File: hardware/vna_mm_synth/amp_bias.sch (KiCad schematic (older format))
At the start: 108 parts, among them U201 LTC2937, U202 NCP692, U203 ADP7158, U204 LM2776, U205 LTM4622A, U206 TPS22918, U207 TPS22918, U208 TPS22918, U209 TPS72301DB, U210 TPS72301DB, U211 TPS72301DB

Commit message: changed synth midband filter bank to admv8416, added rf test points
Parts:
- removed R234: 0, Resistors_SMD:R_0402, symbol Device:R_Small
- added R252, R253: DNI, Resistors_SMD:R_0402, symbol Device:R_Small
- C1120, C1121: DIST_PN (none) -> 399-5514-1-ND
- C229, C230, C231: value C_Small -> 1 uF
- C235, C236, C237: value C_Small -> DNI
- D201: DIST_PN (none) -> 511-1581-1-ND‎
- L201, L202: value L_Small -> BLM15GG471
- R1119: value JMP -> 0
- R1120: value TBD -> 7.5k
- R1122: value TBD -> 12k
- R240, R241, R242: value R_Small -> 10k
- R243, R244, R245: value R_Small -> 1k
- R246, R250: value R_Small -> 68k
- R247: value R_Small -> 21k; DIST_PN (none) -> 311-21.0KLRCT-ND‎
- R248: value R_Small -> 51k
- R249: value R_Small -> 47k
- R251: value R_Small -> 39k
- U201: DIST_PN (none) -> ‎LTC2937CUHE#PBF-ND‎
- U202: DIST_PN (none) -> NCP692MN50T2GOSCT-ND
- U203: DIST_PN (none) -> ADP7158ACPZ-3.3-R7CT-ND‎
- U204: footprint Package_TO_SOT_SMD:SOT-23-6 -> TO_SOT_Packages_SMD:SOT-23-6; DIST_PN (none) -> 296-43957-1-ND
- U205: DIST_PN (none) -> ‎LTM4622AEY#PBF-ND‎
- U206, U207, U208: DIST_PN (none) -> 296-46278-1-ND
- U209, U210, U211: DIST_PN (none) -> ‎296-46478-1-ND‎
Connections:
- net GND: now also R252.2, R253.2
- net PMIC_SDA: no longer R1103.2, U201.19 (SCL)
- net at U204.1 (VOUT): now also C1111.2, C1115.2, L202.2, R236.1
- net at U201.6 (ASEL1): now also R252.1
- net at U201.8 (ASEL3): now also R253.1
- new net PMIC_SCL: R1103.2, U201.19 (SCL)
- no-connect marks 6 -> 4
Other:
- note added: "Rfb = 60.4k * (0.6 / (Vout - 0.6))"

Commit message: added trl cal and set of breakout boards
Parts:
- renumbered C1112 to C1110, C1114 to C1111, C1118 to C1112, C1116 to C1113, C1113 to C1114, C1117 to C1115, C1110 to C1116, C1119 to C1117, C1120 to C1118, C1121 to C1119, C1122 to C1120, C1123 to C1121, C1115 to C1122, C1111 to C1123, C226 to C1126, C227 to C1127, C228 to C1128, C229 to C1129, C230 to C1130, C231 to C1131, C232 to C1132, C233 to C1133, C234 to C1134, C235 to C1135, C236 to C1136, C237 to C1137, C238 to C1138, C239 to C1139, C240 to C1140, C241 to C1141, C242 to C1142, C243 to C1143, D201 to D1101, L201 to L1101, L202 to L1102, R201 to R1101, R252 to R1102, R253 to R1103, R202 to R1104, R1101 to R1105, R1102 to R1106, R1103 to R1107, R1104 to R1108, R1105 to R1109, R1106 to R1110, R1107 to R1111, R210 to R1112, R211 to R1113, R212 to R1114, R213 to R1115, R214 to R1116, R215 to R1117, R216 to R1118, R217 to R1119, R218 to R1120, R219 to R1121, R220 to R1122, R221 to R1123, R222 to R1124, R223 to R1125, R1108 to R1126, R1110 to R1127, R1111 to R1128, R1112 to R1129, R228 to R1130, R1115 to R1131, R1116 to R1132, R1117 to R1133, R1118 to R1134, R1119 to R1135, R1120 to R1136, R236 to R1137, R1121 to R1138, R1122 to R1139, R239 to R1140, R240 to R1141, R241 to R1142, R242 to R1143, R243 to R1144, R244 to R1145, R245 to R1146, R246 to R1147, R247 to R1148, R248 to R1149, R249 to R1150, R250 to R1151, R251 to R1152, U201 to U1101, U202 to U1102, U203 to U1103, U204 to U1104, U205 to U1105, U206 to U1106, U207 to U1107, U208 to U1108, U209 to U1109, U210 to U1110, U211 to U1111

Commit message: added values for divider resistors for negative voltage monitoring, generated interactive BOMs for maam-011109 bias and sequencing breakout boards
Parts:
- R1118: value TBD -> 100k
- R1119: value TBD -> 51k
- R1120, R1122, R1124: value TBD -> 10k
- R1121, R1123: value TBD -> 21k
- R1125: value TBD -> 47k
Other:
- note added: "TODO: FIX EN/V PAIRINGS"
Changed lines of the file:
@@
 U 1 1 5D771187
 P 8800 8850
-F 0 "R1120" V 8900 8950 50  0000 C CNN
-F 1 "TBD" V 8700 8850 50  0000 C CNN
+F 0 "R1120" V 8700 9050 50  0000 C CNN
+F 1 "10k" V 8700 8800 50  0000 C CNN
 F 2 "Resistors_SMD:R_0402" H 8800 8850 50  0001 C CNN
 F 3 "~" H 8800 8850 50  0001 C CNN
@@
 U 1 1 5D7A498E
 P 9050 8850
-F 0 "R1122" V 9150 8950 50  0000 C CNN
-F 1 "TBD" V 8950 8850 50  0000 C CNN
+F 0 "R1122" V 8950 9050 50  0000 C CNN
+F 1 "10k" V 8950 8800 50  0000 C CNN
 F 2 "Resistors_SMD:R_0402" H 9050 8850 50  0001 C CNN
 F 3 "~" H 9050 8850 50  0001 C CNN
@@
 U 1 1 5D7A4C58
 P 9350 8850
-F 0 "R1124" V 9450 8950 50  0000 C CNN
-F 1 "TBD" V 9250 8850 50  0000 C CNN
+F 0 "R1124" V 9250 9050 50  0000 C CNN
+F 1 "10k" V 9250 8800 50  0000 C CNN
 F 2 "Resistors_SMD:R_0402" H 9350 8850 50  0001 C CNN
 F 3 "~" H 9350 8850 50  0001 C CNN
@@
 U 1 1 5D9813CA
 P 8800 9600
-F 0 "R1121" V 8900 9700 50  0000 C CNN
-F 1 "TBD" V 8700 9600 50  0000 C CNN
+F 0 "R1121" V 8700 9450 50  0000 C CNN
+F 1 "21k" V 8700 9750 50  0000 C CNN
 F 2 "Resistors_SMD:R_0402" H 8800 9600 50  0001 C CNN
 F 3 "~" H 8800 9600 50  0001 C CNN
@@
 U 1 1 5D9813D0
 P 9050 9600
-F 0 "R1123" V 9150 9700 50  0000 C CNN
-F 1 "TBD" V 8950 9600 50  0000 C CNN
+F 0 "R1123" V 8950 9450 50  0000 C CNN
+F 1 "21k" V 8950 9750 50  0000 C CNN
 F 2 "Resistors_SMD:R_0402" H 9050 9600 50  0001 C CNN
 F 3 "~" H 9050 9600 50  0001 C CNN
@@
 U 1 1 5D9813D6
 P 9350 9600
-F 0 "R1125" V 9450 9700 50  0000 C CNN
-F 1 "TBD" V 9250 9600 50  0000 C CNN
+F 0 "R1125" V 9250 9450 50  0000 C CNN
+F 1 "47k" V 9250 9750 50  0000 C CNN
 F 2 "Resistors_SMD:R_0402" H 9350 9600 50  0001 C CNN
 F 3 "~" H 9350 9600 50  0001 C CNN
@@
 U 1 1 5DB018C0
 P 8550 8850
-F 0 "R1118" V 8650 8950 50  0000 C CNN
-F 1 "TBD" V 8450 8850 50  0000 C CNN
+F 0 "R1118" V 8450 9050 50  0000 C CNN
+F 1 "100k" V 8450 8800 50  0000 C CNN
 F 2 "Resistors_SMD:R_0402" H 8550 8850 50  0001 C CNN
 F 3 "~" H 8550 8850 50  0001 C CNN
@@
 U 1 1 5DB71176
 P 8550 9600
-F 0 "R1119" V 8650 9700 50  0000 C CNN
-F 1 "TBD" V 8450 9600 50  0000 C CNN
+F 0 "R1119" V 8450 9450 50  0000 C CNN
+F 1 "51k" V 8450 9750 50  0000 C CNN
 F 2 "Resistors_SMD:R_0402" H 8550 9600 50  0001 C CNN
 F 3 "~" H 8550 9600 50  0001 C CNN
@@
 Text Notes 14750 14100 0    50   ~ 0
 Rfb = 60.4k * (0.6 / (Vout - 0.6))
+Text Notes 7300 7250 0    118  ~ 24
+TODO: FIX EN/V PAIRINGS
 $EndSCHEMATC

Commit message: fixed mirrored 3.3V regulator on sequencer board, created and assigned footprints for synth
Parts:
- added R1153, R1154, R1155: 2k, Resistors_SMD:R_0402, symbol Device:R_Small
- R1112, R1113, R1114, R1115, R1116, R1117: value TBD -> 10k
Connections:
- net PGOOD is gone; now on net M5V_EN: R1117.1, U1101.14 (EN6)
- net +3V3: now also U1103.1 (VOUT), U1103.2 (VOUT); no longer U1103.10 (VIN), U1103.9 (VIN)
- net +3V8: now also U1103.10 (VIN), U1103.9 (VIN); no longer U1103.1 (VOUT), U1103.2 (VOUT)
- net -2V5: now also R1154.1
- net -3V3: now also R1155.1
- net -5V: now also R1153.1
- net 3V3_EN: now also R1112.1, U1101.9 (EN1); no longer R1115.1, U1101.12 (EN4)
- net 5V_EN: now also R1113.1, U1101.10 (EN2); no longer R1116.1, U1101.13 (EN5)
- net GND: now also R1153.2, R1154.2, R1155.2
- net M2_5V_EN: now also R1115.1, U1101.12 (EN4); no longer R1113.1, U1101.10 (EN2)
- net M3_5V_EN: now also R1116.1, U1101.13 (EN5); no longer R1114.1, U1101.11 (EN3)
- net M5V_EN: no longer R1112.1, U1101.9 (EN1)
- net at C1106.2: now also U1103.8 (VREG); no longer U1103.3 (VOUT_SENSE)
- net at U1103.7 (REF): now also C1107.2, U1103.6 (REF_SENSE); no longer C1115.2
- net at R1135.2: now also U1103.3 (VOUT_SENSE); no longer U1103.8 (VREG)
- net at R1132.2: now also U1103.5 (EN); no longer U1103.6 (REF_SENSE)
- new net: C1115.2, U1103.4 (BYP)
- new net PGOOD_9V: R1114.1, U1101.11 (EN3)
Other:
- note removed: "TODO: FIX EN/V PAIRINGS"
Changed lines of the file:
@@
 Text Label 19700 2450 2    50   ~ 0
 M5V_EN
-Text Label 7450 8200 0    50   ~ 0
+Text Label 7450 8700 0    50   ~ 0
 M5V_EN
-Text Label 7450 8300 0    50   ~ 0
+Text Label 7450 8500 0    50   ~ 0
 M2_5V_EN
 Text Label 19700 6850 2    50   ~ 0
 M3_5V_EN
-Text Label 7450 8400 0    50   ~ 0
+Text Label 7450 8600 0    50   ~ 0
 M3_5V_EN
 Text Label 13050 6050 3    50   ~ 0
 3V3_EN
-Text Label 7450 8500 0    50   ~ 0
+Text Label 7450 8200 0    50   ~ 0
 3V3_EN
 Text Label 11350 1700 2    50   ~ 0
 5V_EN
-Text Label 7450 8600 0    50   ~ 0
+Text Label 7450 8300 0    50   ~ 0
 5V_EN
 $Comp
@@
 	1    0    0    -1
 $EndComp
-Text HLabel 7450 8700 2    50   Output ~ 0
-PGOOD
+Text HLabel 7450 8400 2    50   Output ~ 0
+PGOOD_9V
 $Comp
 L power:+3.3VP #PWR01110
@@
 P 6450 7850
 F 0 "R1114" V 6550 7950 50  0000 C CNN
-F 1 "TBD" V 6350 7850 50  0000 C CNN
+F 1 "10k" V 6350 7850 50  0000 C CNN
 F 2 "Resistors_SMD:R_0402" H 6450 7850 50  0001 C CNN
 F 3 "~" H 6450 7850 50  0001 C CNN
@@
 P 6700 7850
 F 0 "R1115" V 6800 7950 50  0000 C CNN
-F 1 "TBD" V 6600 7850 50  0000 C CNN
+F 1 "10k" V 6600 7850 50  0000 C CNN
 F 2 "Resistors_SMD:R_0402" H 6700 7850 50  0001 C CNN
 F 3 "~" H 6700 7850 50  0001 C CNN
@@
 P 6950 7850
 F 0 "R1116" V 7050 7950 50  0000 C CNN
-F 1 "TBD" V 6850 7850 50  0000 C CNN
+F 1 "10k" V 6850 7850 50  0000 C CNN
 F 2 "Resistors_SMD:R_0402" H 6950 7850 50  0001 C CNN
 F 3 "~" H 6950 7850 50  0001 C CNN
@@
 P 6200 7850
 F 0 "R1113" V 6300 7950 50  0000 C CNN
-F 1 "TBD" V 6100 7850 50  0000 C CNN
+F 1 "10k" V 6100 7850 50  0000 C CNN
 F 2 "Resistors_SMD:R_0402" H 6200 7850 50  0001 C CNN
 F 3 "~" H 6200 7850 50  0001 C CNN
@@
 P 7200 7850
 F 0 "R1117" V 7300 7950 50  0000 C CNN
-F 1 "TBD" V 7100 7850 50  0000 C CNN
+F 1 "10k" V 7100 7850 50  0000 C CNN
 F 2 "Resistors_SMD:R_0402" H 7200 7850 50  0001 C CNN
 F 3 "~" H 7200 7850 50  0001 C CNN
@@
 P 5950 7850
 F 0 "R1112" V 6050 7950 50  0000 C CNN
-F 1 "TBD" V 5850 7850 50  0000 C CNN
+F 1 "10k" V 5850 7850 50  0000 C CNN
 F 2 "Resistors_SMD:R_0402" H 5950 7850 50  0001 C CNN
 F 3 "~" H 5950 7850 50  0001 C CNN
@@
 F 4 "ADP7158ACPZ-3.3-R7CT-ND‎" H 12250 4350 50  0001 C CNN "DIST_PN"
 	1    12250 4350
-	1    0    0    -1
+	-1   0    0    -1
 $EndComp
 $Comp
@@
 Text Notes 14750 14100 0    50   ~ 0
 Rfb = 60.4k * (0.6 / (Vout - 0.6))
-Text Notes 7300 7250 0    118  ~ 24
-TODO: FIX EN/V PAIRINGS
+$Comp
+L Device:R_Small R1153
+U 1 1 5E08B417
+P 22400 2450
+F 0 "R1153" H 22500 2500 50  0000 C CNN
+F 1 "2k" H 22500 2400 50  0000 C CNN
+F 2 "Resistors_SMD:R_0402" H 22400 2450 50  0001 C CNN
+F 3 "~" H 22400 2450 50  0001 C CNN
+	1    22400 2450
+	1    0    0    -1
+$EndComp
+$Comp
+L power:GND #PWR0102
+U 1 1 5E08BA04
+P 22400 2650
+F 0 "#PWR0102" H 22400 2400 50  0001 C CNN
+F 1 "GND" H 22405 2477 50  0000 C CNN
+F 2 "" H 22400 2650 50  0001 C CNN
+F 3 "" H 22400 2650 50  0001 C CNN
+	1    22400 2650
+	1    0    0    -1
+$EndComp
+Wire Wire Line
+	22400 2550 22400 2650
+Wire Wire Line
+	21800 2250 22400 2250
+Wire Wire Line
+	22400 2250 22400 2350
+$Comp
+L Device:R_Small R1154
+U 1 1 5E142CA4
+P 22400 4700
+F 0 "R1154" H 22500 4750 50  0000 C CNN
+F 1 "2k" H 22500 4650 50  0000 C CNN
+F 2 "Resistors_SMD:R_0402" H 22400 4700 50  0001 C CNN
+F 3 "~" H 22400 4700 50  0001 C CNN
+	1    22400 4700
+	1    0    0    -1
+$EndComp
+$Comp
+L power:GND #PWR0103
+U 1 1 5E142CAA
+P 22400 4900
+F 0 "#PWR0103" H 22400 4650 50  0001 C CNN
+F 1 "GND" H 22405 4727 50  0000 C CNN
+F 2 "" H 22400 4900 50  0001 C CNN
+F 3 "" H 22400 4900 50  0001 C CNN
+	1    22400 4900
+	1    0    0    -1
+$EndComp
+Wire Wire Line
+	22400 4800 22400 4900
+Wire Wire Line
+	21800 4500 22400 4500
+Wire Wire Line
+	22400 4500 22400 4600
+$Comp
+L Device:R_Small R1155
+U 1 1 5E180174
+P 22400 6850
+F 0 "R1155" H 22500 6950 50  0000 C CNN
+F 1 "2k" H 22500 6850 50  0000 C CNN
+F 2 "Resistors_SMD:R_0402" H 22400 6850 50  0001 C CNN
+F 3 "~" H 22400 6850 50  0001 C CNN
+	1    22400 6850
+	1    0    0    -1
+$EndComp
+$Comp
+L power:GND #PWR0104
+U 1 1 5E18017A
+P 22400 7050
+F 0 "#PWR0104" H 22400 6800 50  0001 C CNN
+F 1 "GND" H 22405 6877 50  0000 C CNN
+F 2 "" H 22400 7050 50  0001 C CNN
+F 3 "" H 22400 7050 50  0001 C CNN
+	1    22400 7050
+	1    0    0    -1
+$EndComp
+Wire Wire Line
+	22400 6950 22400 7050
+Wire Wire Line
+	21800 6650 22400 6650
+Wire Wire Line
+	22400 6650 22400 6750
 $EndSCHEMATC

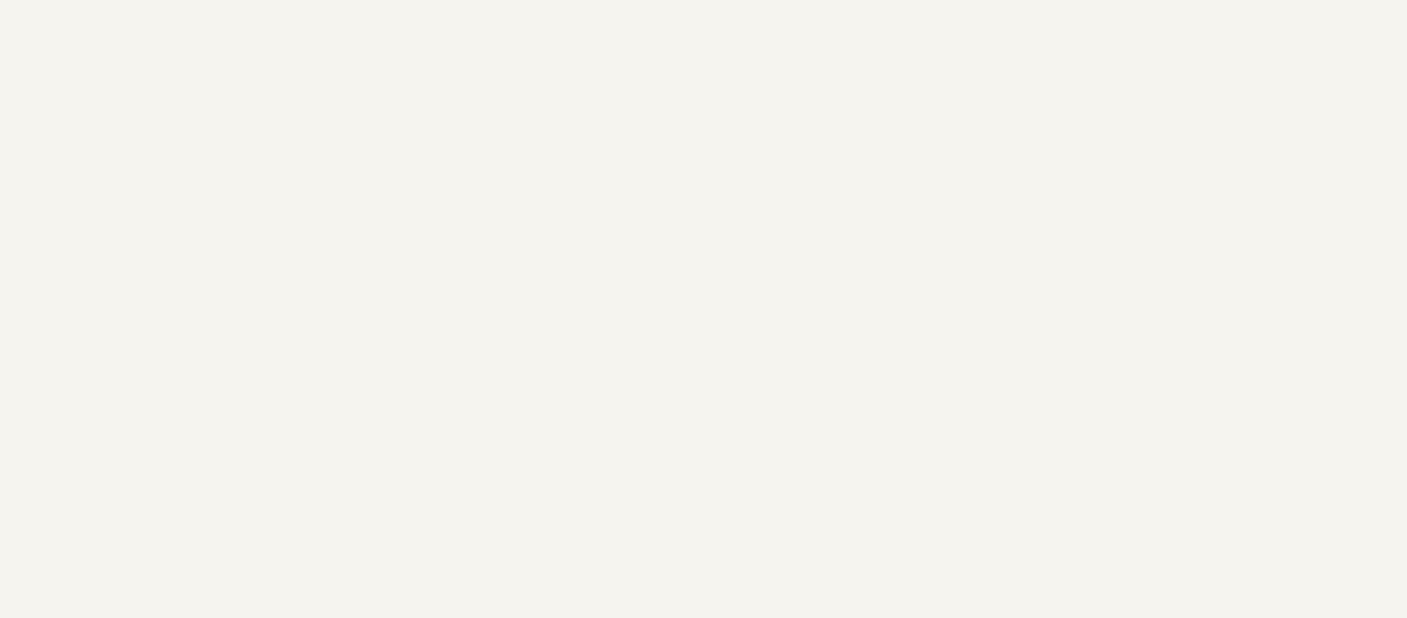
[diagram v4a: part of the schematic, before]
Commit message: started variable filter bias circuitry - added 15V bias
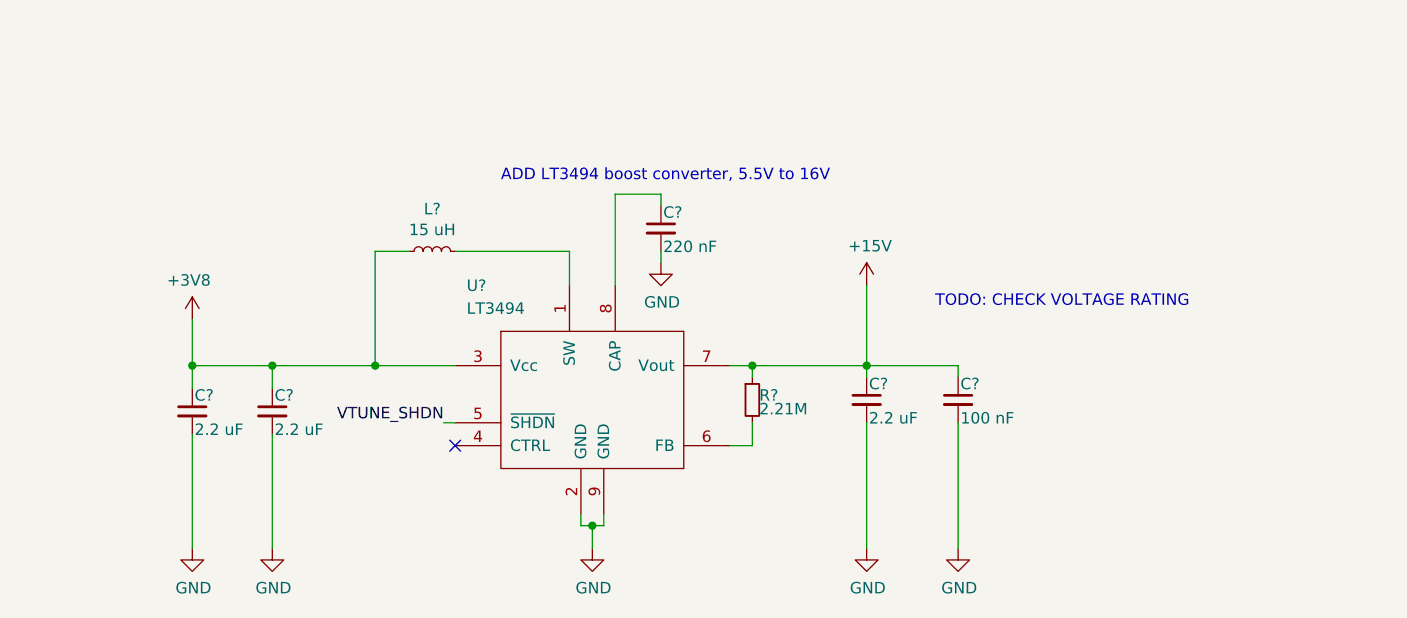
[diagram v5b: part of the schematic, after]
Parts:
- added C? (x3): 2.2 uF, Capacitors_SMD:C_0603, symbol Device:C_Small
- added C?: 220 nF, Capacitors_SMD:C_0603, symbol Device:C_Small
- added C?: 100 nF, Capacitors_SMD:C_0603, symbol Device:C_Small
- added L?: 15 uH, symbol device:L_Small
- added R?: 2.21M, Resistors_SMD:R_0402, symbol Device:R_Small
- added U?: LT3494, symbol vna_mm:LT3494
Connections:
- net +3V8: now also C?.1, C?.1, L?.1, U?.3 (Vcc)
- net GND: now also C?.2, C?.2, C?.2, C?.2, C?.2, U?.2 (GND), U?.9 (GND)
- new net: L?.2, U?.1 (SW)
- new net: R?.2, U?.6 (FB)
- new net: C?.1, U?.8 (CAP)
- new net +15V: C?.1, C?.1, R?.1, U?.7 (Vout)
- new net VTUNE_SHDN: U?.5 (~SHDN)
- no-connect marks 4 -> 5
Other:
- note added: "ADD LT3494 boost converter, 5.5V to 16V"
- note added: "TODO: CHECK VOLTAGE RATING"

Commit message: started separate reference clock generation board
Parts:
- added R? (x2): 10k, Resistors_SMD:R_0402, symbol Device:R_Small
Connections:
- net +5VP: now also R?.1
- net GND: now also R?.2
- net VTUNE_SHDN: now also R?.1, R?.2
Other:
- note added: "SEQUENCE ON AFTER +/- 5V ARE ENABLED"
- note added: "TODO: ADD REVERSE POLARITY, OVERCURRENT, AND OVERVOLTAGE PROTECTION TO 9V INPUT"
- note removed: "ADD LT3494 boost converter, 5.5V to 16V"
- moved on the sheet: C?, L?, R?, U?

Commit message: cleanup and update vna mm synth schematic for modern kicad libraries
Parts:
- C1101, C1104, C1105, C1108, C1111, C1113, C1117, C1120, C1121, C1126, C1127, C1128, C1141, C1142, C1143: footprint Capacitors_SMD:C_0603 -> Capacitor_SMD:C_0603_1608Metric
- C1102, C1103, C1106, C1107, C1109, C1110, C1112, C1114, C1115, C1116, C1122, C1123, C1124, C1125, C1129, C1130, C1131, C1132, C1133, C1134, C1135, C1136, C1137, C1138, C1139, C1140: footprint Capacitors_SMD:C_0402 -> Capacitor_SMD:C_0402_1005Metric
- C1118, C1119: footprint Capacitors_SMD:C_1210 -> Capacitor_SMD:C_1210_3225Metric
- C1144, C1145, C1146, C1147, C1148: renamed from C?; footprint Capacitors_SMD:C_0603 -> Capacitor_SMD:C_0603_1608Metric
- D1101: footprint LEDs:LED_0603 -> LED_SMD:LED_0603_1608Metric
- L1101, L1102: footprint Resistors_SMD:R_0402 -> Inductor_SMD:L_0402_1005Metric
- L1103: renamed from L?; symbol device:L_Small -> Device:L_Small
- R1101, R1102, R1103, R1104, R1105, R1106, R1107, R1108, R1109, R1110, R1111, R1112, R1113, R1114, R1115, R1116, R1117, R1118, R1119, R1120, R1121, R1122, R1123, R1124, R1125, R1126, R1127, R1128, R1129, R1130, R1131, R1132, R1133, R1134, R1135, R1136, R1137, R1138, R1139, R1140, R1141, R1142, R1143, R1144, R1145, R1146, R1147, R1148, R1149, R1150, R1151, R1152, R1153, R1154, R1155: footprint Resistors_SMD:R_0402 -> Resistor_SMD:R_0402_1005Metric
- R1156, R1157, R1158: renamed from R?; footprint Resistors_SMD:R_0402 -> Resistor_SMD:R_0402_1005Metric
- gave numbers to parts that had none: 1

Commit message: footprint assignment
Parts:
- L1103: footprint (none) -> Inductor_SMD:L_1210_3225Metric
- U1102: footprint Housings_DFN_QFN:DFN-6-1EP_3x3mm_Pitch0.95mm -> Package_DFN_QFN:DFN-6-1EP_3x3mm_P0.95mm_EP1.7x2.6mm
- U1103: footprint Housings_DFN_QFN:DFN-10-1EP_3x3mm_Pitch0.5mm -> Package_DFN_QFN:DFN-10-1EP_3x3mm_P0.5mm_EP1.65x2.38mm
- U1104, U1106, U1107, U1108: footprint TO_SOT_Packages_SMD:SOT-23-6 -> Package_TO_SOT_SMD:SOT-23-6
- U1109, U1110, U1111: footprint TO_SOT_Packages_SMD:SOT-23-5 -> Package_TO_SOT_SMD:SOT-23-5
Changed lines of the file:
@@
 F 0 "U1108" H 20100 12265 50  0000 C CNN
 F 1 "TPS22918" H 20100 12174 50  0000 C CNN
-F 2 "TO_SOT_Packages_SMD:SOT-23-6" H 20050 12350 50  0001 C CNN
+F 2 "Package_TO_SOT_SMD:SOT-23-6" H 20050 12350 50  0001 C CNN
 F 3 "http://www.ti.com/lit/ds/symlink/tps22918.pdf" H 20100 12100 50  0001 C CNN
 F 4 "296-46278-1-ND" H 20100 11800 50  0001 C CNN "DIST_PN"
@@
 F 0 "U1107" H 20100 10715 50  0000 C CNN
 F 1 "TPS22918" H 20100 10624 50  0000 C CNN
-F 2 "TO_SOT_Packages_SMD:SOT-23-6" H 20050 10800 50  0001 C CNN
+F 2 "Package_TO_SOT_SMD:SOT-23-6" H 20050 10800 50  0001 C CNN
 F 3 "http://www.ti.com/lit/ds/symlink/tps22918.pdf" H 20100 10550 50  0001 C CNN
 F 4 "296-46278-1-ND" H 20100 10250 50  0001 C CNN "DIST_PN"
@@
 F 0 "U1106" H 20100 9065 50  0000 C CNN
 F 1 "TPS22918" H 20100 8974 50  0000 C CNN
-F 2 "TO_SOT_Packages_SMD:SOT-23-6" H 20050 9150 50  0001 C CNN
+F 2 "Package_TO_SOT_SMD:SOT-23-6" H 20050 9150 50  0001 C CNN
 F 3 "http://www.ti.com/lit/ds/symlink/tps22918.pdf" H 20100 8900 50  0001 C CNN
 F 4 "296-46278-1-ND" H 20100 8600 50  0001 C CNN "DIST_PN"
@@
 F 0 "U1109" H 20300 2715 50  0000 C CNN
 F 1 "TPS72301DB" H 20300 2624 50  0000 C CNN
-F 2 "TO_SOT_Packages_SMD:SOT-23-5" H 20300 2850 50  0001 C CNN
+F 2 "Package_TO_SOT_SMD:SOT-23-5" H 20300 2850 50  0001 C CNN
 F 3 "http://www.ti.com/lit/ds/symlink/tps723.pdf" H 20300 2450 50  0001 C CNN
 F 4 "‎296-46478-1-ND‎" H 20300 2350 50  0001 C CNN "DIST_PN"
@@
 F 0 "U1102" H 12250 1915 50  0000 C CNN
 F 1 "NCP692" H 12250 1824 50  0000 C CNN
-F 2 "Housings_DFN_QFN:DFN-6-1EP_3x3mm_Pitch0.95mm" H 11600 2250 50  0001 C CNN
+F 2 "Package_DFN_QFN:DFN-6-1EP_3x3mm_P0.95mm_EP1.7x2.6mm" H 11600 2250 50  0001 C CNN
 F 3 "https://www.onsemi.com/pub/Collateral/NCP690-D.PDF" H 12250 1600 50  0001 C CNN
 F 4 "NCP692MN50T2GOSCT-ND" H 12250 1550 50  0001 C CNN "DIST_PN"
@@
 F 0 "U1110" H 20300 4965 50  0000 C CNN
 F 1 "TPS72301DB" H 20300 4874 50  0000 C CNN
-F 2 "TO_SOT_Packages_SMD:SOT-23-5" H 20300 5100 50  0001 C CNN
+F 2 "Package_TO_SOT_SMD:SOT-23-5" H 20300 5100 50  0001 C CNN
 F 3 "http://www.ti.com/lit/ds/symlink/tps723.pdf" H 20300 4700 50  0001 C CNN
 F 4 "‎296-46478-1-ND‎" H 20300 4600 50  0001 C CNN "DIST_PN"
@@
 F 0 "U1111" H 20300 7115 50  0000 C CNN
 F 1 "TPS72301DB" H 20300 7024 50  0000 C CNN
-F 2 "TO_SOT_Packages_SMD:SOT-23-5" H 20300 7250 50  0001 C CNN
+F 2 "Package_TO_SOT_SMD:SOT-23-5" H 20300 7250 50  0001 C CNN
 F 3 "http://www.ti.com/lit/ds/symlink/tps723.pdf" H 20300 6850 50  0001 C CNN
 F 4 "‎296-46478-1-ND‎" H 20300 6750 50  0001 C CNN "DIST_PN"
@@
 F 0 "U1104" H 13500 8850 50  0000 L CNN
 F 1 "LM2776" H 13500 8750 50  0000 L CNN
-F 2 "TO_SOT_Packages_SMD:SOT-23-6" H 13200 8600 50  0001 L CNN
+F 2 "Package_TO_SOT_SMD:SOT-23-6" H 13200 8600 50  0001 L CNN
 F 3 "http://www.ti.com/lit/ds/symlink/lm2776.pdf" H 11300 10200 50  0001 C CNN
 F 4 "296-43957-1-ND" H 13150 8950 50  0001 C CNN "DIST_PN"
@@
 F 0 "U1103" H 12250 4837 60  0000 C CNN
 F 1 "ADP7158" H 12250 4731 60  0000 C CNN
-F 2 "Housings_DFN_QFN:DFN-10-1EP_3x3mm_Pitch0.5mm" H 12250 4350 60  0001 C CNN
+F 2 "Package_DFN_QFN:DFN-10-1EP_3x3mm_P0.5mm_EP1.65x2.38mm" H 12250 4350 60  0001 C CNN
 F 3 "https://www.analog.com/media/en/technical-documentation/data-sheets/ADP7158.pdf" H 12250 4350 60  0001 C CNN
 F 4 "ADP7158ACPZ-3.3-R7CT-ND‎" H 12250 4350 50  0001 C CNN "DIST_PN"
@@
 F 0 "L1103" V 6485 13300 50  0000 C CNN
 F 1 "15 uH" V 6394 13300 50  0000 C CNN
-F 2 "" H 6300 13300 60  0001 C CNN
+F 2 "Inductor_SMD:L_1210_3225Metric" H 6300 13300 60  0001 C CNN
 F 3 "" H 6300 13300 60  0000 C CNN
 	1    6300 13300
